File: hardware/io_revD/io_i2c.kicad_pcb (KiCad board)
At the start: 2 copper layers, 85.7 x 76.8 mm, 37 parts, among them J1 Target Interface, 2716 Pinout, J2 Jumper Block, J3 Jumper Block, J4 Target Interface, 2716 Pinout, Q1 2N7000, U1 2716, U2 74HCT74, U3 74HCT125, U4 74HCT138, U5 74LS04, U6 MCP23018-E_SP, U7 74HCT138

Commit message: board edit for revD, not done yet
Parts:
- moved U7 130.6 mm to (86.1, 146.1)
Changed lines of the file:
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@@
   )
   (footprint "Package_DIP:DIP-16_W7.62mm" (layer "F.Cu")
-    (at 210.82 107.188)
+    (at 86.116 146.065)
     (descr "16-lead though-hole mounted DIP package, row spacing 7.62 mm (300 mils)")
     (tags "THT DIP DIL PDIP 2.54mm 7.62mm 300mil")

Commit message: revD board
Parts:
- removed the REF** at (101.6, 95.9)
- removed the REF** at (179.7, 95.9)
- removed the REF** at (101.6, 165.1)
- removed the REF** at (179.7, 165.1)
- removed U5: 74LS04, Package_DIP:DIP-14_W7.62mm
- added D10: 1N4148, Diode_THT:D_DO-35_SOD27_P2.54mm_Vertical_AnodeUp, F.Cu at (115.1, 155.4)
- added D11: 1N4148, Diode_THT:D_DO-35_SOD27_P2.54mm_Vertical_AnodeUp, F.Cu at (105.9, 155.4)
- added D12: 1N4148, Diode_THT:D_DO-35_SOD27_P2.54mm_Vertical_AnodeUp, F.Cu at (103.4, 155.4)
- added D13: 1N4148, Diode_THT:D_DO-35_SOD27_P2.54mm_Vertical_AnodeUp, F.Cu at (100.8, 155.4)
- added D14: 1N4148, Diode_THT:D_DO-35_SOD27_P2.54mm_Vertical_AnodeUp, F.Cu at (98.3, 155.4)
- added D15: 1N4148, Diode_THT:D_DO-35_SOD27_P2.54mm_Vertical_AnodeUp, F.Cu at (95.8, 155.4)
- added D16: 1N4148, Diode_THT:D_DO-35_SOD27_P2.54mm_Vertical_AnodeUp, F.Cu at (90.7, 155.4)
- added D17: 1N4148, Diode_THT:D_DO-35_SOD27_P2.54mm_Vertical_AnodeUp, F.Cu at (87.4, 155.4)
- added J10: Conn_01x01, Connector_PinHeader_2.54mm:PinHeader_1x01_P2.54mm_Vertical, F.Cu at (162.1, 114.3)
- added J11: Conn_01x01, Connector_PinHeader_2.54mm:PinHeader_1x01_P2.54mm_Vertical, F.Cu at (162.1, 124.5)
- added J12: Conn_01x01, Connector_PinHeader_2.54mm:PinHeader_1x01_P2.54mm_Vertical, F.Cu at (96.3, 98.8)
- added J13: Conn_01x01, Connector_PinHeader_2.54mm:PinHeader_1x01_P2.54mm_Vertical, F.Cu at (133.3, 98.8)
- added J14: Conn_01x01, Connector_PinHeader_2.54mm:PinHeader_1x01_P2.54mm_Vertical, F.Cu at (133.3, 103.9)
- added J15: Conn_01x01, Connector_PinHeader_2.54mm:PinHeader_1x01_P2.54mm_Vertical, F.Cu at (157.7, 105.9)
- added J5: Conn_01x01, Connector_PinHeader_2.54mm:PinHeader_1x01_P2.54mm_Vertical, F.Cu at (175.5, 163.6)
- added J6: Conn_01x01, Connector_PinHeader_2.54mm:PinHeader_1x01_P2.54mm_Vertical, F.Cu at (173.0, 163.6)
- added J7: Conn_01x01, Connector_PinHeader_2.54mm:PinHeader_1x01_P2.54mm_Vertical, F.Cu at (178.1, 163.6)
- added J8: Conn_01x01, Connector_PinHeader_2.54mm:PinHeader_1x01_P2.54mm_Vertical, F.Cu at (162.1, 109.2)
- added J9: Conn_01x01, Connector_PinHeader_2.54mm:PinHeader_1x01_P2.54mm_Vertical, F.Cu at (162.1, 111.8)
- added R6: 4.7k, Resistor_THT:R_Axial_DIN0207_L6.3mm_D2.5mm_P2.54mm_Vertical, F.Cu at (128.3, 136.9)
- added R7: 1k, Resistor_THT:R_Axial_DIN0207_L6.3mm_D2.5mm_P2.54mm_Vertical, F.Cu at (138.9, 155.4)
- added R8: 10k, Resistor_THT:R_Axial_DIN0207_L6.3mm_D2.5mm_P2.54mm_Vertical, F.Cu at (162.3, 133.3)
- added REF**: MountingHole_3.2mm_M3, MountingHole:MountingHole_3.2mm_M3, F.Cu at (184.7, 97.3)
- added REF**: MountingHole_3.2mm_M3, MountingHole:MountingHole_3.2mm_M3, F.Cu at (88.1, 97.3)
- added REF**: MountingHole_3.2mm_M3, MountingHole:MountingHole_3.2mm_M3, F.Cu at (88.1, 165.1)
- added REF**: MountingHole_3.2mm_M3, MountingHole:MountingHole_3.2mm_M3, F.Cu at (184.7, 165.1)
- D1, D2: value 1N4148 -> 1N4004; footprint Diode_THT:D_DO-35_SOD27_P2.54mm_Vertical_AnodeUp -> Diode_THT:D_DO-41_SOD81_P2.54mm_Vertical_AnodeUp
- D8, D9: value 1N4004 -> 1N4148; footprint Diode_THT:D_DO-41_SOD81_P2.54mm_Vertical_AnodeUp -> Diode_THT:D_DO-35_SOD27_P2.54mm_Vertical_AnodeUp
- Q1: footprint Package_TO_SOT_THT:TO-92_Inline -> Package_TO_SOT_THT:TO-92_Wide
- R2, R3: value 1k -> 4.7k
- moved C5 77.3 mm to (87.4, 152.8), turned to 90 degrees
- moved R3 70.8 mm to (182.9, 143.3), turned to 0 degrees
- moved D2 68.4 mm to (160.3, 98.0), turned to 0 degrees
- moved C6 66.3 mm to (183.6, 125.5), turned to -90 degrees
- moved D9 57.5 mm to (117.6, 155.4), turned to -90 degrees
- moved C2 56.9 mm to (139.2, 152.8), turned to 90 degrees
- moved D8 55.6 mm to (120.1, 155.4)
- moved R1 50.3 mm to (159.0, 155.7), turned to 0 degrees
- moved J2 49.5 mm to (155.4, 157.7), turned to -90 degrees
- moved C4 48.6 mm to (150.9, 98.9)
- moved U3 45.7 mm to (165.3, 160.5)
- moved D1 45.3 mm to (105.7, 98.8), turned to 180 degrees
- moved C3 44.4 mm to (183.9, 153.0)
- moved R2 41.7 mm to (182.9, 148.6), turned to 0 degrees
- moved J3 35.3 mm to (171.7, 147.8), turned to 90 degrees
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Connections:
- A1 pad 10: /WR enable -> unconnected-(A1-Pad10)
- A1 pad 11: unconnected-(A1-Pad11) -> /SCL2
- A1 pad 12: unconnected-(A1-Pad12) -> /SDA2
- A1 pad 19: unconnected-(A1-Pad19) -> Net-(A1-Pad19)
- A1 pad 20: unconnected-(A1-Pad20) -> Net-(A1-Pad20)
- A1 pad 21: unconnected-(A1-Pad21) -> Net-(A1-Pad21)
- A1 pad 25: unconnected-(A1-Pad25) -> Net-(A1-Pad25)
- D1 pad 1: Net-(D1-Pad1) -> +5V
- D1 pad 2: /program OE -> +5VD
- D2 pad 1: Net-(D2-Pad1) -> +5V
- D2 pad 2: /program OE -> +5VA
- D3 pad 1: Net-(D3-Pad1) -> /program OE
- D3 pad 2: /program OE -> Net-(D10-Pad2)
- D4 pad 2: /program OE -> Net-(D10-Pad2)
- D5 pad 2: /program OE -> Net-(D10-Pad2)
- D6 pad 2: /program OE -> Net-(D10-Pad2)
- D7 pad 2: /program OE -> Net-(D10-Pad2)
- D8 pad 1: +5V -> Net-(D8-Pad1)
- D8 pad 2: +5VD -> Net-(D10-Pad2)
- D9 pad 1: +5V -> Net-(D9-Pad1)
- D9 pad 2: +5VA -> Net-(D10-Pad2)
- R2 pad 1: +5V -> Net-(J3-Pad5)
- R2 pad 2: /program OE -> GND
- R3 pad 1: +5V -> Net-(J3-Pad6)
- R3 pad 2: Net-(R3-Pad2) -> GND
- U1 pad 20: /program OE -> Net-(D10-Pad2)
- U1 pad 21: Net-(R3-Pad2) -> /program WR
- U2 pad 11: Net-(U2-Pad11) -> Net-(D16-Pad1)
- U2 pad 3: Net-(U2-Pad11) -> Net-(D16-Pad1)
- U3 pad 10: GND -> /Target CE
- U3 pad 11: unconnected-(U3-Pad11) -> Net-(J3-Pad6)
- U3 pad 12: GND -> +5VD
- U3 pad 13: GND -> /Target OE
- U3 pad 4: /WR enable -> Net-(J6-Pad1)
- U3 pad 5: /program WR -> Net-(J5-Pad1)
- U3 pad 6: Net-(R3-Pad2) -> Net-(J7-Pad1)
- U3 pad 8: unconnected-(U3-Pad8) -> Net-(J3-Pad5)
- U3 pad 9: GND -> +5VD
- U4 pad 10: Net-(D5-Pad1) -> Net-(D9-Pad1)
- U4 pad 11: Net-(U3-Pad1) -> Net-(D8-Pad1)
- U4 pad 12: Net-(D4-Pad1) -> Net-(D7-Pad1)
- U4 pad 13: Net-(D3-Pad1) -> Net-(D6-Pad1)
- U4 pad 14: Net-(D2-Pad1) -> Net-(D5-Pad1)
- U4 pad 15: Net-(D1-Pad1) -> Net-(D4-Pad1)
- U4 pad 4: Net-(J3-Pad4) -> Net-(J3-Pad3)
- U4 pad 5: Net-(J3-Pad3) -> Net-(J3-Pad4)
- U4 pad 7: Net-(D7-Pad1) -> Net-(U4-Pad7)
- U4 pad 9: Net-(D6-Pad1) -> Net-(D10-Pad1)
- U7 pad 1: unconnected-(U7-Pad1) -> /A5
- U7 pad 10: unconnected-(U7-Pad10) -> Net-(U3-Pad1)
- U7 pad 11: unconnected-(U7-Pad11) -> Net-(D15-Pad1)
- U7 pad 12: unconnected-(U7-Pad12) -> Net-(D14-Pad1)
- U7 pad 13: unconnected-(U7-Pad13) -> Net-(D13-Pad1)
- U7 pad 14: unconnected-(U7-Pad14) -> Net-(D12-Pad1)
- U7 pad 15: unconnected-(U7-Pad15) -> Net-(D11-Pad1)
- U7 pad 16: unconnected-(U7-Pad16) -> +5V
- U7 pad 2: unconnected-(U7-Pad2) -> /A6
- U7 pad 3: unconnected-(U7-Pad3) -> /A7
- U7 pad 4: unconnected-(U7-Pad4) -> GND
- U7 pad 5: unconnected-(U7-Pad5) -> Net-(U4-Pad7)
- U7 pad 6: unconnected-(U7-Pad6) -> +5V
- U7 pad 7: unconnected-(U7-Pad7) -> Net-(D17-Pad1)
- U7 pad 8: unconnected-(U7-Pad8) -> GND
- U7 pad 9: unconnected-(U7-Pad9) -> Net-(D16-Pad1)
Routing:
- net /WR enable: track 105.5 -> 0.00 mm, vias 3 -> 0
- net Net-(D10-Pad2): track 0.00 -> 104.4 mm, vias 0 -> 1
- net /A7: track 44.3 -> 124.6 mm, vias 0 -> 2
- net Net-(D16-Pad1): track 0.00 -> 73.7 mm, vias 0 -> 2
- net /A6: track 44.3 -> 117.1 mm, vias 0 -> 2
- net Net-(R3-Pad2): track 71.4 -> 0.00 mm
- net Net-(J2-Pad5): track 94.1 -> 23.6 mm, vias 1 -> 0
- net /SDA2: track 0.00 -> 65.5 mm, vias 0 -> 1
- net /A5: track 44.5 -> 109.3 mm, vias 0 -> 2
- net Net-(U3-Pad1): track 20.5 -> 84.2 mm, vias 0 -> 2
- net +5VD: track 92.9 -> 153.4 mm, vias 1 -> 2
- net /SCL2: track 0.00 -> 59.9 mm, vias 0 -> 1
- net Net-(J2-Pad3): track 54.5 -> 11.5 mm, vias 1 -> 0
- net /Target OE: track 72.0 -> 115.0 mm, vias 0 -> 2
- net Net-(J2-Pad1): track 63.0 -> 21.1 mm
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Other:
- board size 85.7 x 76.8 mm -> 103.6 x 74.9 mm
- board text added: "1"
- board text added: "1N4148 or similar"
- board text added: "2716 or 2816 goes here"
- board text added: "5v Arduino"
- board text added: "5v Combined"
- board text added: "5v Target"
- board text added: "A0"
- board text added: "A1"
- board text added: "A2"
- board text added: "A6"
- board text added: "Active High"
- board text added: "Active Low"
- board text added: "All capacitors 100nF"
- board text added: "Demon Debugger Rev. D Knarfian Labs Frank Palazzolo Evan Allen"
- board text added: "Disconnect target and J2 jumpers for programming"
- board text added: "Gnd"
- board text added: "Ground"
- board text added: "In"
- board text added: "Jumper across all J2 pads for ROM-mapped I/O"
- board text added: "Minimal interface is the arduino, Q1, R4, and R5 connected out J2"
- board text added: "Out"
- board text added: "Program WR cap (to prevent spurious writes?)"
- board text added: "Ribbon to DIP socket"
- board text added: "SCL"
- board text added: "Trig"
- board text added: "U6, C4, and U1 being a 2816 enables onboard reprogramming of the flash chip"
- board text added: "socket for stacking goes on back"
- board text removed: "Demon Debugger Rev. C Knarfian Labs Frank Palazzolo Evan Allen"
- board text removed: "GND"
- board text removed: "Invert"
- board text removed: "Norm"
- board text removed: "SCK"
- board text removed: "WR cap"
- board text removed: "unhook from target and unhook i2c jumpers when programming"
- board text removed: "use 28C16 for programming"

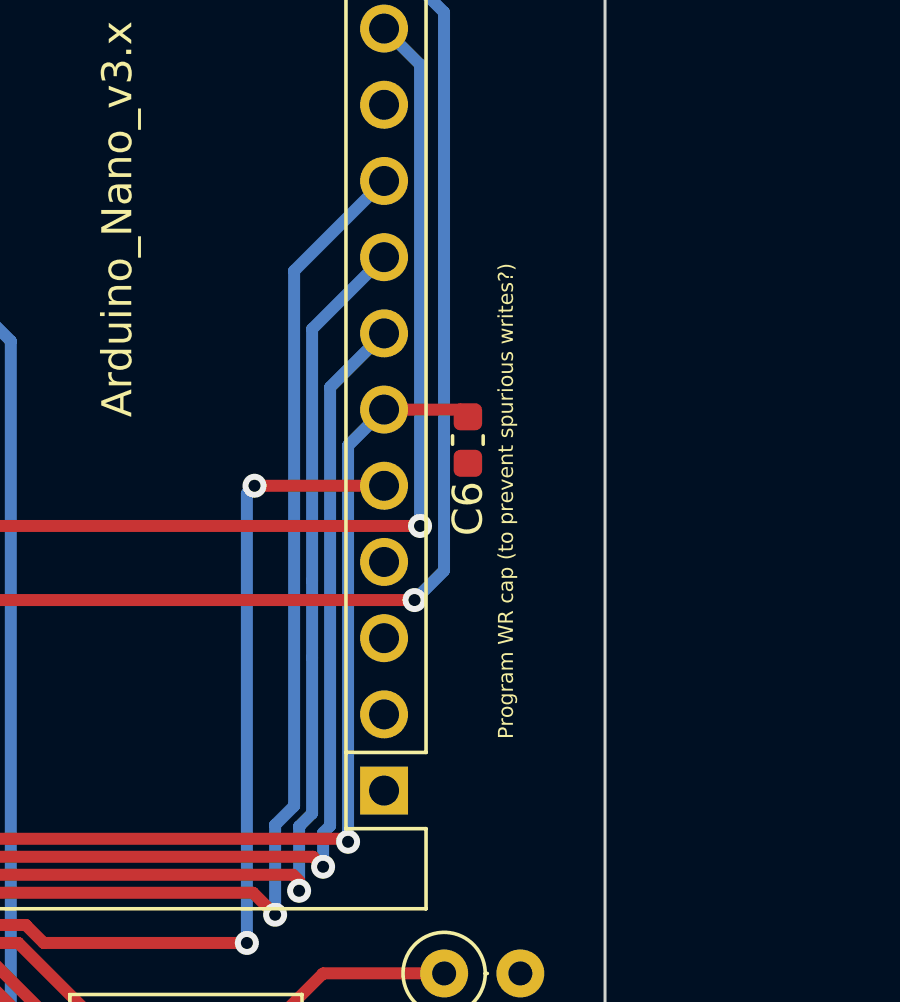
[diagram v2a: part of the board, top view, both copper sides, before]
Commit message: Remove C6, Updated warning label, new pdf
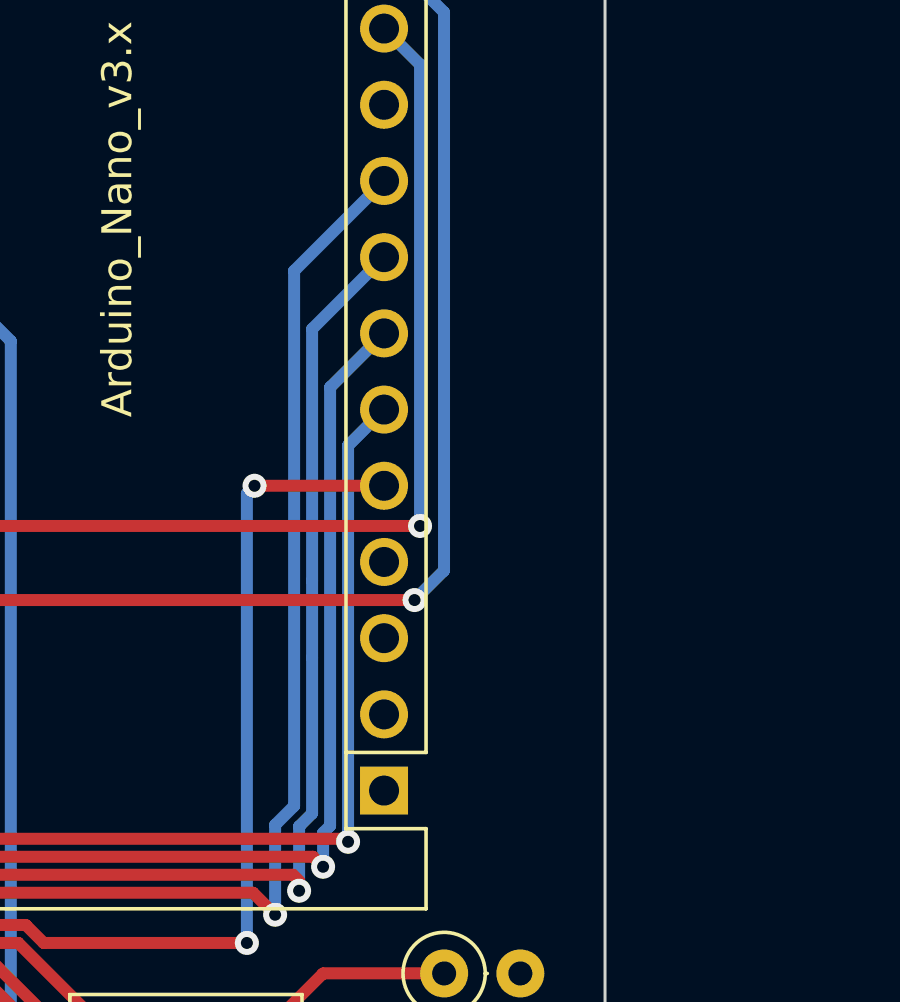
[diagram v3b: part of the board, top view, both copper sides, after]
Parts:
- removed C6: 0.1uF, Capacitor_SMD:C_0603_1608Metric
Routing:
- net /program WR: track 100.5 -> 97.7 mm
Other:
- board text added: "Disconnect target for programming"
- board text removed: "Disconnect target and J2 jumpers for programming"
- board text removed: "Program WR cap (to prevent spurious writes?)"
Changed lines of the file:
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@@
     (pad "" np_thru_hole circle locked (at 0 0) (size 3.2 3.2) (drill 3.2) (layers *.Cu *.Mask))
   )
-  (footprint "Capacitor_SMD:C_0603_1608Metric" (layer "F.Cu")
-    (at 183.642 125.476 -90)
-    (descr "Capacitor SMD 0603 (1608 Metric), square (rectangular) end terminal, IPC_7351 nominal, (Body size source: IPC-SM-782 page 76, https://www.pcb-3d.com/wordpress/wp-content/uploads/ipc-sm-782a_amendment_1_and_2.pdf), generated with kicad-footprint-generator")
-    (tags "capacitor")
-    (property "Sheetfile" "io_i2c.kicad_sch")
-    (property "Sheetname" "")
-    (attr smd)
-    (fp_text reference "C6" (at 2.286 0 90) (layer "F.SilkS")
-      (effects (font (size 1 1) (thickness 0.15)))
-    )
-    (fp_text value "0.1uF" (at 0 1.43 90) (layer "F.Fab")
-      (effects (font (size 1 1) (thickness 0.15)))
-    )
-    (fp_text user "${REFERENCE}" (at 0 0 90) (layer "F.Fab")
-      (effects (font (size 0.4 0.4) (thickness 0.06)))
-    )
-    (fp_line (start -0.14058 0.51) (end 0.14058 0.51) (layer "F.SilkS") (width 0.12))
-    (fp_line (start -0.14058 -0.51) (end 0.14058 -0.51) (layer "F.SilkS") (width 0.12))
-    (fp_line (start 1.48 0.73) (end -1.48 0.73) (layer "F.CrtYd") (width 0.05))
-    (fp_line (start -1.48 0.73) (end -1.48 -0.73) (layer "F.CrtYd") (width 0.05))
-    (fp_line (start -1.48 -0.73) (end 1.48 -0.73) (layer "F.CrtYd") (width 0.05))
-    (fp_line (start 1.48 -0.73) (end 1.48 0.73) (layer "F.CrtYd") (width 0.05))
-    (fp_line (start -0.8 -0.4) (end 0.8 -0.4) (layer "F.Fab") (width 0.1))
-    (fp_line (start 0.8 0.4) (end -0.8 0.4) (layer "F.Fab") (width 0.1))
-    (fp_line (start -0.8 0.4) (end -0.8 -0.4) (layer "F.Fab") (width 0.1))
-    (fp_line (start 0.8 -0.4) (end 0.8 0.4) (layer "F.Fab") (width 0.1))
-    (pad "1" smd roundrect locked (at -0.775 0 270) (size 0.9 0.95) (layers "F.Cu" "F.Paste" "F.Mask") (roundrect_rratio 0.25)
-      (net 42 "/program WR") (pintype "passive"))
-    (pad "2" smd roundrect locked (at 0.775 0 270) (size 0.9 0.95) (layers "F.Cu" "F.Paste" "F.Mask") (roundrect_rratio 0.25)
-      (net 1 "GND") (pintype "passive"))
-    (model "${KICAD6_3DMODEL_DIR}/Capacitor_SMD.3dshapes/C_0603_1608Metric.wrl"
-      (offset (xyz 0 0 0))
-      (scale (xyz 1 1 1))
-      (rotate (xyz 0 0 0))
-    )
-  )
   (footprint "Package_DIP:DIP-24_W15.24mm_Socket" (layer "F.Cu")
     (at 86.614 102.108)
@@
     (effects (font (size 1 1) (thickness 0.15)) (justify mirror))
   )
-  (gr_text "Disconnect target and J2 jumpers for programming" (at 151.638 142.494) (layer "B.SilkS")
+  (gr_text "Disconnect target for programming" (at 151.638 142.494) (layer "B.SilkS")
     (effects (font (size 1 1) (thickness 0.15)) (justify mirror))
   )
@@
     (effects (font (size 0.7 0.7) (thickness 0.1)))
   )
-  (gr_text "Program WR cap (to prevent spurious writes?)" (at 184.912 127.508 90) (layer "F.SilkS")
-    (effects (font (size 0.5 0.5) (thickness 0.05)))
-  )
   (gr_text "Demon Debugger\nRev. D\nKnarfian Labs\nFrank Palazzolo\nEvan Allen" (at 115.824 138.938) (layer "F.SilkS")
     (effects (font (size 1 1) (thickness 0.15)))
@@
   (segment (start 132.98956 138.646489) (end 132.371511 138.646489) (width 0.4) (layer "F.Cu") (net 42))
   (segment (start 133.096 138.752929) (end 132.98956 138.646489) (width 0.4) (layer "F.Cu") (net 42))
-  (segment (start 180.848 124.46) (end 183.401 124.46) (width 0.4) (layer "F.Cu") (net 42))
   (segment (start 179.648489 138.867511) (end 179.549 138.768022) (width 0.4) (layer "F.Cu") (net 42))
   (segment (start 125.759 136.906) (end 127.499489 138.646489) (width 0.4) (layer "F.Cu") (net 42))
-  (segment (start 183.401 124.46) (end 183.642 124.701) (width 0.4) (layer "F.Cu") (net 42))
   (via (at 179.648489 138.867511) (size 0.8) (drill 0.4) (layers "F.Cu" "B.Cu") (net 42))
   (segment (start 127.254 109.728) (end 125.454969 111.527031) (width 0.4) (layer "B.Cu") (net 42))

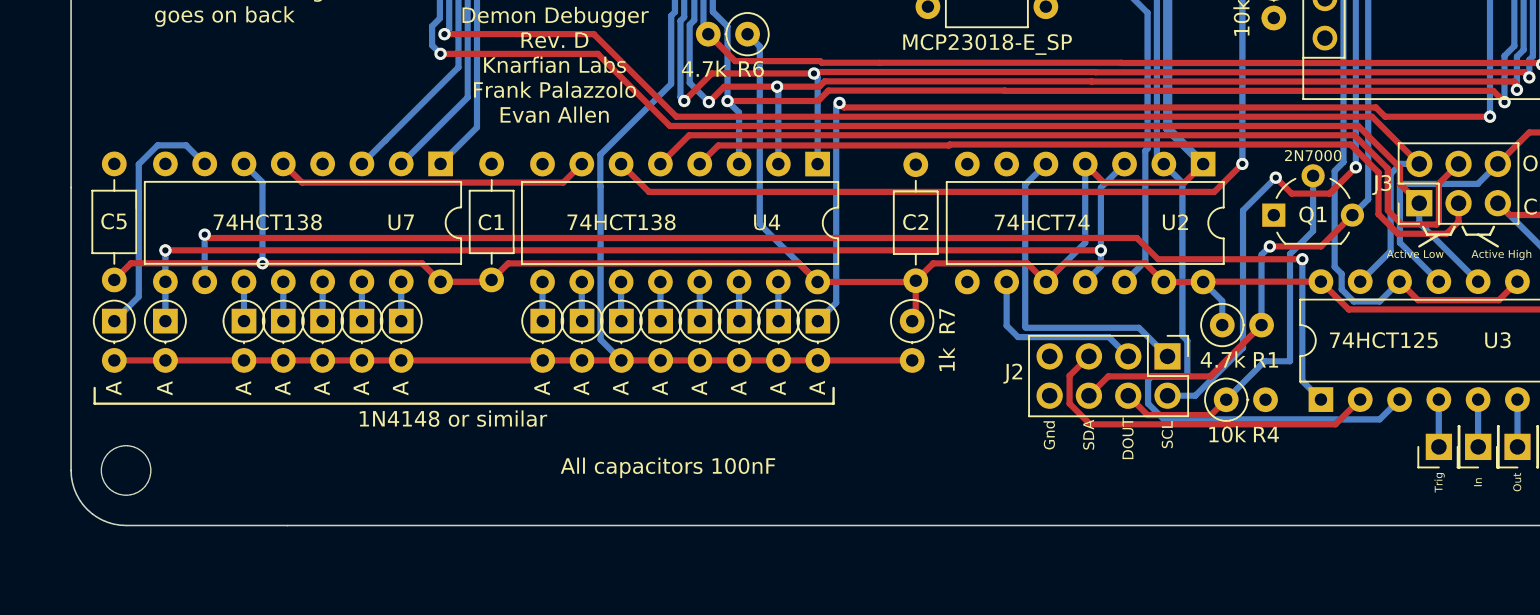
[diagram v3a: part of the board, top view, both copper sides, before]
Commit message: added silk regions, labeling, jumper for rom emulator mode
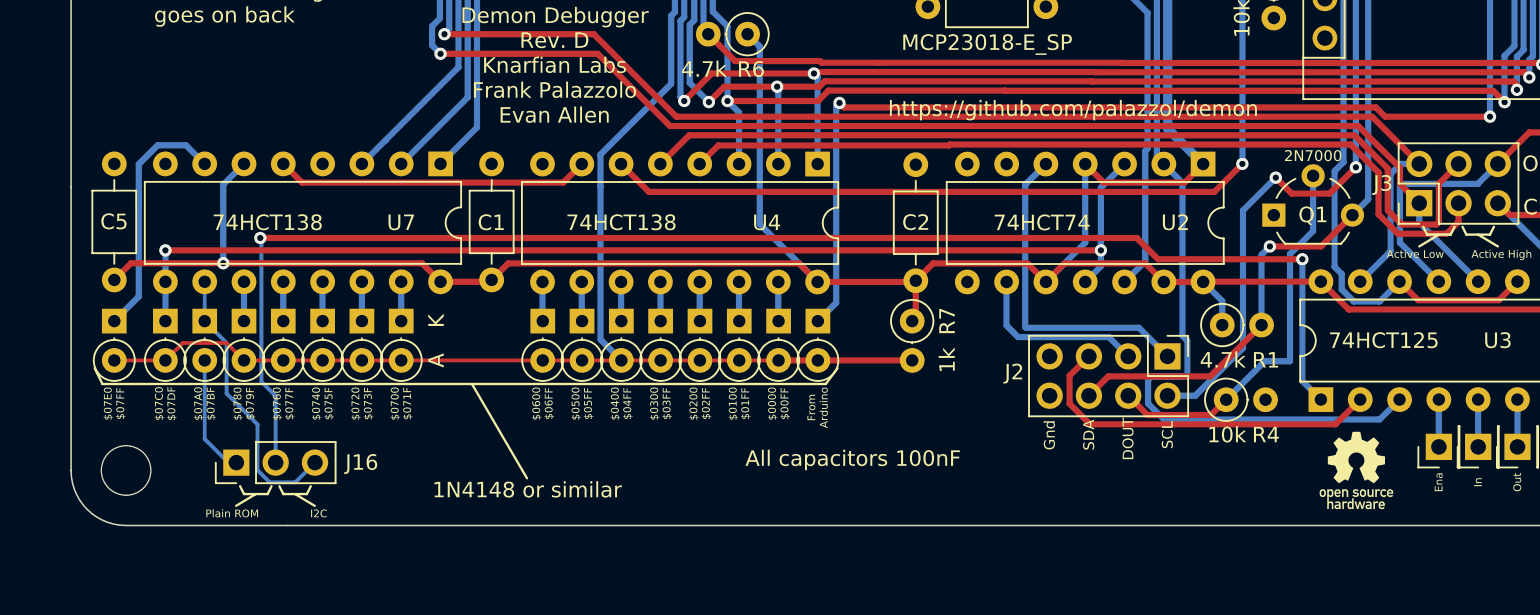
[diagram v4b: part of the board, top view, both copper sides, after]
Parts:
- added D18: 1N4148, Diode_THT:D_DO-35_SOD27_P2.54mm_Vertical_KathodeUp, F.Cu at (93.2, 155.4)
- added G***: LOGO, Evan's misc parts:OSHW gear, F.Cu at (167.6, 165.1)
- added G***: LOGO, Evan's misc parts:Evan Logo, B.Cu at (142.7, 161.3)
- added J16: read region, Connector_PinHeader_2.54mm:PinHeader_1x03_P2.54mm_Vertical, F.Cu at (95.3, 164.6)
- D10, D11, D12, D13, D14, D15, D16, D17, D3, D4, D5, D6, D7, D8, D9: footprint Diode_THT:D_DO-35_SOD27_P2.54mm_Vertical_AnodeUp -> Diode_THT:D_DO-35_SOD27_P2.54mm_Vertical_KathodeUp
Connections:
- U7 pad 10: Net-(U3-Pad1) -> Net-(U7-Pad10)
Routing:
- net Net-(U7-Pad10): track 0.00 -> 18.1 mm
- net Net-(U3-Pad1): track 84.2 -> 92.4 mm
- net Net-(D18-Pad2): track 0.00 -> 7.76 mm
- net Net-(D10-Pad2): track 104.4 -> 107.9 mm
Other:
- board text added: "$0000 $00FF"
- board text added: "$0100 $01FF"
- board text added: "$0200 $02FF"
- board text added: "$0300 $03FF"
- board text added: "$0400 $04FF"
- board text added: "$0500 $05FF"
- board text added: "$0600 $06FF"
- board text added: "$0700 $071F"
- board text added: "$0720 $073F"
- board text added: "$0740 $075F"
- board text added: "$0760 $077F"
- board text added: "$0780 $079F"
- board text added: "$07A0 $07BF"
- board text added: "$07C0 $07DF"
- board text added: "$07E0 $07FF"
- board text added: "Ena"
- board text added: "From Arduino"
- board text added: "I2C"
- board text added: "Plain ROM"
- board text added: "abzman2k.wordpress.com"
- board text added: "avoidspikes.blogspot.com"
- board text added: "https://github.com/palazzol/demon"
- board text removed: "Trig"
